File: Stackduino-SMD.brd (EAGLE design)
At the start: 62.5 x 68 mm, 65 parts

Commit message: latest progress on brd v2.1
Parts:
- removed BWD, FWD, MENU_SEL: JST-PH_2-PIN_HEADER, SRG:JST_B2B-PH_HEADER
- removed ENCODER: JST-PH_3-PIN_HEADER, SRG:JST_B3B-PH_HEADER
- removed ICSP: AVR-ISP-6, avr-5:AVR-ISP-6
- added CON1: B4B-ZR, jst-connectors:B4B-ZR
- added U$1: B5B-ZR, jst-connectors:B5B-ZR
- CAM: value JST-PH_3-PIN_HEADER -> B3B-ZR; device SRG:JST_B3B-PH_HEADER -> jst-connectors:B3B-ZR
- U$2: value OLED Display -> B9B-ZR; device Stackduino:DIGOLE_OLED -> jst-connectors:B9B-ZR
- moved H2 78.9 mm to (3.00, 71.0), turned to 180 degrees
- moved H1 78.4 mm to (57.0, 71.0), turned to 180 degrees
- moved 12VDC 76.0 mm to (52.7, 14.9), turned to 180 degrees
- moved USB 74.4 mm to (8.00, 17.0), turned to 90 degrees
- moved H4 70.1 mm to (3.00, 24.2), turned to 180 degrees
- moved H3 63.9 mm to (57.0, 29.0), turned to 180 degrees
- moved L1 62.7 mm to (51.4, 64.3), turned to 180 degrees
- moved R9 61.3 mm to (9.20, 23.6), turned to 0 degrees
- moved D2 58.3 mm to (55.5, 57.8), turned to 90 degrees
- moved CAM 58.0 mm to (11.8, 66.3), turned to 180 degrees
- moved DB15 57.6 mm to (30.0, 17.0), turned to 180 degrees
- moved C8 54.2 mm to (10.1, 39.0), turned to 180 degrees
- moved D1 54.1 mm to (52.6, 29.4), turned to 90 degrees
- moved C10 53.9 mm to (15.3, 29.6)
- moved FT232RL 53.8 mm to (8.45, 32.5), turned to 270 degrees
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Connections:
- removed net N$11: ATMEGA328P.29, C8.1, ICSP.5, R10.1
- new net +5V: U$2.9
- new net RESET: ATMEGA328P.29, C8.1, R10.1, U$2.8
- net BWD: now also CON1.1; no longer BWD.P1
- net CAM_GND: now also CAM.2; no longer CAM.P3
- net ENCSWITCH: now also U$1.5; no longer MENU_SEL.P1
- net ENC_A: now also U$1.1; no longer ENCODER.P1
- net ENC_B: now also U$1.3; no longer ENCODER.P3
- net FWD: now also CON1.3; no longer FWD.P1
- net GND: now also CON1.2, CON1.4, U$1.2, U$1.4, U$2.1; no longer BWD.P2, ENCODER.P2, FWD.P2, ICSP.6, MENU_SEL.P2, U$2.GND@1, U$2.GND@2
- net MISO: now also U$2.6; no longer ICSP.1
- net MOSI: now also U$2.5; no longer ICSP.4
- net N$22: now also U$2.4; no longer U$2.SS
- net N$23: now also U$2.2; no longer U$2.DATA
- net N$24: now also U$2.3; no longer U$2.CLK
- net OPT1: now also CAM.3; no longer CAM.P2
- net OPT2: now also CAM.1; no longer CAM.P1
- net OUT1A: now also A4988_CARRIER.1B; no longer A4988_CARRIER.1A
- net OUT1B: now also A4988_CARRIER.1A; no longer A4988_CARRIER.1B
- net SCK: now also U$2.7; no longer ICSP.3
- net VCC: no longer ICSP.2, U$2.VCC
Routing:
- net VCC: track 457.0 -> 26.8 mm, vias 10 -> 0
- net DIG2: track 146.4 -> 0.00 mm, vias 2 -> 0
- net PBUTTON: track 87.4 -> 0.00 mm, vias 1 -> 0
- net DIG1: track 72.9 -> 0.00 mm, vias 2 -> 0
- net V+: track 86.9 -> 14.4 mm, vias 6 -> 0
- net KILL: track 70.4 -> 0.00 mm, vias 2 -> 0
- net LIM2: track 65.1 -> 0.00 mm, vias 1 -> 0
- net N$11: track 64.8 -> 0.00 mm, vias 2 -> 0
- net STAT: track 57.8 -> 0.00 mm, vias 2 -> 0
- net LIM1: track 56.4 -> 0.00 mm, vias 1 -> 0
- net OPT1: track 68.5 -> 13.8 mm
- net OPT2: track 72.0 -> 21.1 mm
- net N$19: track 49.4 -> 0.00 mm, vias 2 -> 0
- net STEP: track 49.1 -> 0.00 mm
- net CAM_GND: track 67.0 -> 18.1 mm, vias 1 -> 0
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- removed copper zone on layer 1, net VIN
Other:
- board size 62.5 x 68 mm -> 60 x 62 mm

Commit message: latest progress
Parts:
- removed DIG_IO: JST-PH_2-PIN_HEADER, SRG:JST_B2B-PH_HEADER
- added BLUETOOTH: B4B-ZR, jst-connectors:B4B-ZR
- added MP4: NTR4501N, sym:SOT23
- added R18: 2K, eagle-ltspice:R0805
- added R19: 150 Ohm, eagle-ltspice:R0805
- added R22: 10K, eagle-ltspice:R0805
- ON/OFF, START/STOP: value JST-PH_2-PIN_HEADER -> B2B-ZR; device SRG:JST_B2B-PH_HEADER -> jst-connectors:B2B-ZR
- R11: value 10K -> 1K
- moved START/STOP 24.6 mm to (42.0, 72.0)
- moved R5 22.2 mm to (45.0, 51.0)
- moved R3 21.9 mm to (8.45, 55.6)
- moved R11 21.2 mm to (34.0, 52.0), turned to 0 degrees
- moved R4 15.7 mm to (10.4, 55.6)
- moved R12 13.3 mm to (6.50, 41.3), turned to 270 degrees
- moved ON/OFF 12.8 mm to (41.8, 27.9), turned to 180 degrees
- moved R7 12.5 mm to (10.2, 69.8)
- moved OPT1 12.0 mm to (10.2, 66.0), turned to 90 degrees
- moved C13 11.8 mm to (22.4, 66.0)
- moved R6 11.7 mm to (16.5, 63.5), turned to 90 degrees
- moved C1 11.2 mm to (44.5, 28.9), turned to 180 degrees
- moved R14 10.5 mm to (24.4, 53.2)
- moved C5 10.5 mm to (6.50, 50.4), turned to 270 degrees
- moved CAM 10.2 mm to (2.54, 62.2), turned to 90 degrees
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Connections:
- removed net EXTRA_INPUT: DIG_IO.P1, MCP23017.28
- new net BLUETOOTH_ENABLE: MCP23017.28, R19.1
- new net MCU_RX: ATMEGA328P.30, BLUETOOTH.1, FT232RL.1
- new net MCU_TX: ATMEGA328P.31, BLUETOOTH.2, R11.2, R18.1
- new net N$11: FT232RL.5, R11.1
- net GND: now also BLUETOOTH.3, ON/OFF.2, R18.2, R22.1, START/STOP.2; no longer DIG_IO.P2, ON/OFF.P2, START/STOP.P2
- net N$13: now also MP4.1, R19.2, R22.2; no longer ATMEGA328P.31, FT232RL.5
- net N$14: now also BLUETOOTH.4, MP4.2; no longer ATMEGA328P.30, FT232RL.1
- net OPT1: now also CAM.1; no longer CAM.3
- net OPT2: now also CAM.3; no longer CAM.1
- net PBUTTON: now also ON/OFF.1; no longer ON/OFF.P1, R11.1
- net START_STOP: now also START/STOP.1; no longer START/STOP.P1
- net V+: no longer R11.2
- net VCC: now also MP4.3
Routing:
- net VCC: track 26.8 -> 121.5 mm
- net LIM1: track 0.00 -> 46.3 mm
- net CAM_GND: track 18.1 -> 61.2 mm
- net LIM2: track 0.00 -> 42.2 mm
- net STEP: track 0.00 -> 41.6 mm, vias 0 -> 1
- net MCU_RX: track 0.00 -> 41.3 mm, vias 0 -> 1
- net OPT1: track 13.8 -> 52.4 mm, vias 1 -> 0
- net DIR: track 0.00 -> 37.8 mm, vias 0 -> 1
- net DIG1: track 0.00 -> 35.6 mm, vias 0 -> 1
- net DIG2: track 0.00 -> 35.0 mm, vias 0 -> 1
- net ENCSWITCH: track 0.00 -> 34.0 mm, vias 0 -> 1
- net N$11: track 0.00 -> 32.7 mm, vias 0 -> 1
- net OPT2: track 21.1 -> 53.6 mm, vias 1 -> 0
- net N$19: track 0.00 -> 31.8 mm, vias 0 -> 2
- net N$18: track 0.00 -> 30.0 mm, vias 0 -> 2
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
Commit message: topside board nearly complete
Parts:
- removed LTC2950: LTC2950CTS8-1TRPBF, LTC_By_element14_Batch_1:SOT65P280X100-8N
- removed LTC4412: LTC4412ES6PBF, LTC_By_element14_Batch_1:SOT95P280X100-6N
- removed R0: 470K, eagle-ltspice:R0805
- removed R22: 10K, eagle-ltspice:R0805
- added LTC1: LTC2950CTS8-1TRPBF, LTC_By_element14_Batch_1:SOT65P280X100-8N
- added LTC2: LTC4412ES6PBF, LTC_By_element14_Batch_1:SOT95P280X100-6N
- added R20: 4.7K, eagle-ltspice:R0805
- added R21: 100K, eagle-ltspice:R0805
- C1: value 22uF -> 0.1uF
- C10: value 100nF -> 0.1uF
- C11: value 22pF -> 100uF; device eagle-ltspice:C0805 -> SparkFun-Passives:PANASONIC_D
- C12: value 22pF -> 100nF
- C13: value 0.1uF -> 22uF
- C2: value 100uF -> 22pF; device SparkFun-Passives:PANASONIC_D -> eagle-ltspice:C0805
- C3: value 10nF -> 22pF
- C4: value 68uF -> 10nF; device SparkFun-Passives:PANASONIC_D -> eagle-ltspice:C0805
- C6: value 100uF -> 68uF
- C7: value 0.1uF -> 100uF; device eagle-ltspice:C0805 -> SparkFun-Passives:PANASONIC_D
- MP1: value FDN306P -> NTR4501N
- MP4: value NTR4501N -> FDN306P
- R1, R2: value 100K -> 220 Ohm
- R10, R16: value 10K -> 150 Ohm
- R12: value 10K -> 2K
- R13, R19: value 150 Ohm -> 10K
- R14: value 10K -> 470K
- R15, R3, R9: value 4.7K -> 10K
- R17: value 150 Ohm -> 100K
- R18: value 2K -> 100K
- R4: value 4.7K -> 150 Ohm
- R5: value 100K -> 4.7K
- R6: value 220 Ohm -> 4.7K
- R7: value 220 Ohm -> 10K
- R8: value 10K -> 4.7K
- moved H3 54.2 mm to (3.00, 24.2)
- moved H4 54.2 mm to (57.0, 29.0)
- moved H1 54.0 mm to (3.00, 71.0)
- moved H2 54.0 mm to (57.0, 71.0)
- moved R1 51.7 mm to (10.2, 70.5), turned to 180 degrees
- moved MP4 50.2 mm to (52.0, 38.4), turned to 270 degrees
- moved C13 46.9 mm to (46.9, 26.0), turned to 270 degrees
- moved C12 46.5 mm to (18.5, 28.9), turned to 0 degrees
- moved R2 45.0 mm to (16.5, 63.5), turned to 90 degrees
- moved MP1 44.8 mm to (5.20, 56.4), turned to 0 degrees
- moved C1 43.2 mm to (22.4, 66.0), turned to 90 degrees
- moved R5 36.8 mm to (8.45, 55.6)
- moved R8 33.3 mm to (24.4, 55.6), turned to 0 degrees
- moved R9 33.3 mm to (24.4, 53.2), turned to 180 degrees
- moved R12 32.4 mm to (36.8, 52.8), turned to 90 degrees
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- renumbered CON1 to FWD/BWD, DB15 to DB1, LM2675 to LM1, MCP23017 to MCP1, U$1 to ENCODER, U$2 to ICSP/SPI/OLED
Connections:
- net BATTVIN: now also LTC2.1, MP4.3; no longer LTC4412.1, MP1.3
- net BATT_FET: now also R10.1; no longer R13.1
- net BATT_SENSE: now also R8.2, R9.1; no longer R14.1, R15.2
- net BATT_VOLT: now also MP2.3; no longer MP3.3
- net BLUETOOTH_ENABLE: now also R4.1; no longer R19.1
- net GATE: now also LTC2.5, MP4.1; no longer LTC4412.5, MP1.1
- net GND: now also C11.-, C2.2, C3.2, C7.-, D1.A, LTC1.4, LTC2.2, LTC2.3, R12.2, R19.2, R3.1, R7.1, R8.1; no longer C11.2, C2.-, C4.-, C7.2, D2.A, LTC2950.4, LTC4412.2, LTC4412.3, R15.1, R16.1, R18.2, R22.1, R8.2
- net INT: now also LTC1.5, R18.2; no longer LTC2950.5, R2.2
- net KILL: now also LTC1.8, R21.1; no longer LTC2950.8, R1.1
- net MCU_TX: now also R12.1; no longer R18.1
- net N$1: now also LTC1.6; no longer LTC2950.6
- net N$10: now also MP3.1, R16.1; no longer MP2.1, R17.1
- net N$12: now also MP2.1, R10.2, R7.2; no longer MP3.1, R13.2, R16.2
- net N$13: now also MP1.1, R3.2, R4.2; no longer MP4.1, R19.2, R22.2
- net N$14: now also MP1.2; no longer MP4.2
- net N$16: now also MP2.2, R9.2; no longer MP3.2, R14.2
- net N$18: now also R6.1; no longer R4.1
- net N$19: now also R5.2; no longer R3.2
- net N$2: now also R17.1; no longer R5.1
- net N$30: now also R20.1; no longer R9.1
- net N$34: now also R2.1; no longer R6.1
- net N$36: now also R1.1; no longer R7.1
- net N$4: now also C4.1; no longer C3.1
- net N$43: now also C12.1; no longer C10.1
- net N$44: now also R19.1, R20.2; no longer R8.1, R9.2
- net N$7: now also C4.2, D1.C; no longer C3.2, D2.C
- net N$8: now also R13.1; no longer R12.1
- net N$9: now also C11.+, MP3.2; no longer MP2.2
- net PBUTTON: now also LTC1.2; no longer LTC2950.2
- net PD6: now also R2.2; no longer R6.2
- net PD7: now also R1.2; no longer R7.2
- net RESET: now also R15.1; no longer R10.1
- net STAT: now also LTC2.4, R14.1; no longer LTC4412.4, R0.1
- net V+: now also C13.1, C7.+, D2.C, LTC1.1, LTC2.6, MP3.3, MP4.2; no longer C1.1, C2.+, C6.+, D1.C, LTC2950.1, LTC4412.6, MP1.2, MP2.3
- net VCC: now also C1.1, C10.1, C6.+, MP1.3, R13.2, R14.2, R15.2, R16.2, R18.1, R21.2, R5.1, R6.2; no longer C13.1, C4.+, C7.1, MP4.3, R0.2, R1.2, R10.2, R12.2, R2.1, R3.1, R4.2, R5.2
- net VIN: now also D2.A; no longer D1.A
- net XTAL1: now also C3.1; no longer C11.1
- net XTAL2: now also C2.1; no longer C12.1
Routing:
- net MCU_TX: track 7.92 -> 73.0 mm, vias 0 -> 2
- net RESET: track 7.72 -> 69.4 mm, vias 0 -> 3
- net VCC: track 121.5 -> 180.3 mm, vias 0 -> 4
- net DIG1: track 35.6 -> 1.84 mm, vias 1 -> 0
- net DIG2: track 35.0 -> 1.57 mm, vias 1 -> 0
- net MCU_RX: track 41.3 -> 7.91 mm, vias 1 -> 0
- net ENCSWITCH: track 34.0 -> 2.63 mm, vias 1 -> 0
- net N$11: track 32.7 -> 1.45 mm, vias 1 -> 0
- net N$17: track 27.2 -> 1.47 mm, vias 1 -> 0
- net N$1: track 0.00 -> 24.6 mm, vias 0 -> 2
- net N$14: track 24.0 -> 1.68 mm, vias 1 -> 0
- net PD6: track 32.6 -> 45.6 mm, vias 2 -> 0
- net V+: track 20.9 -> 33.0 mm
- net BATTVIN: track 0.00 -> 11.9 mm
- net GATE: track 0.00 -> 11.1 mm, vias 0 -> 2
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- added copper zone on layer 1, net BATTVIN
- added copper zone on layer 1, net N$9
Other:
- board text removed: "MISO"
- board text removed: "MOSI"
- board text removed: "RST"
- board text removed: "SCK"
- board text removed: "VDD"

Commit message: latest progress
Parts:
- moved R14 7.13 mm to (11.9, 39.6)
- moved C10 3.42 mm to (33.0, 29.8), turned to 270 degrees
- moved CAM 0.46 mm to (3.00, 62.2)
- moved FWD/BWD 0.10 mm to (1.50, 41.2)
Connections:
- net DIG1: now also DB1.14; no longer DB1.13
- net DIG2: now also DB1.13; no longer DB1.14
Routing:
- net DIG2: track 1.57 -> 50.8 mm
- net DIG1: track 1.84 -> 46.6 mm
- net OPT2: track 59.4 -> 68.8 mm
- net OPT1: track 59.6 -> 68.0 mm
- net CAM_GND: track 67.0 -> 73.3 mm
- net N$2: track 5.26 -> 0.00 mm
- net DIR: track 34.6 -> 39.4 mm
- net STEP: track 38.4 -> 42.5 mm
- net LIM1: track 46.3 -> 49.8 mm
- net LIM2: track 42.2 -> 45.6 mm
- net VCC: track 180.3 -> 177.1 mm
- net SLEEP: track 23.9 -> 22.6 mm, vias 0 -> 1
- net MS3: track 18.9 -> 17.8 mm
- net RESET: track 69.4 -> 68.2 mm
- net ENABLE: track 16.6 -> 15.6 mm
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
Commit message: nearly there,,,
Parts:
- moved R14 41.9 mm to (47.0, 16.6), turned to 270 degrees
- moved C8 7.18 mm to (11.1, 39.3), turned to 180 degrees
- moved C9 2.34 mm to (16.6, 32.8), turned to 270 degrees
- moved R17 2.05 mm to (31.8, 36.2)
- moved C12 1.95 mm to (16.6, 28.9), turned to 270 degrees
- moved C10 1.80 mm to (31.8, 31.1), turned to 180 degrees
- moved R4 1.62 mm to (2.27, 51.4)
- moved R7 1.56 mm to (15.2, 55.5), turned to 0 degrees
- moved MP2 1.45 mm to (19.3, 56.6)
- moved FT232RL 1.34 mm to (10.1, 32.8)
- moved C2 0.80 mm to (41.2, 70.3)
- moved C3 0.80 mm to (41.2, 55.2)
- moved H1 0.80 mm to (3.00, 71.8)
- moved H2 0.80 mm to (57.0, 71.8)
- moved START/STOP 0.75 mm to (43.5, 72.2)
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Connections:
- net N$14 renamed BLUETOOTH_VCC
- removed net N$11: FT232RL.5, R11.1
- new net MCU_TX_3_3V: BLUETOOTH.2, FT232RL.5, R11.1
- net DIG1: now also DB1.12; no longer DB1.14
- net DIG2: now also DB1.11; no longer DB1.13
- net ENCSWITCH: now also MCP1.3; no longer MCP1.26
- net INT: now also MCP1.24; no longer MCP1.27
- net KILL: now also MCP1.25; no longer MCP1.3
- net LIM1: now also DB1.13, MCP1.26; no longer DB1.11, MCP1.23
- net LIM2: now also DB1.14, MCP1.27; no longer DB1.12, MCP1.24
- net MCU_TX: no longer BLUETOOTH.2
- net PD6: now also ATMEGA328P.11; no longer ATMEGA328P.10
- net PD7: now also ATMEGA328P.10; no longer ATMEGA328P.11
- net STAT: now also MCP1.23; no longer MCP1.25
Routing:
- net STAT: track 3.96 -> 74.8 mm, vias 0 -> 2
- net BATT_VOLT: track 9.26 -> 76.4 mm
- net ALOG2: track 2.27 -> 67.5 mm, vias 0 -> 1
- net ALOG1: track 2.27 -> 67.1 mm, vias 0 -> 1
- net MCU_TX: track 73.0 -> 8.62 mm, vias 2 -> 0
- net INT: track 6.35 -> 68.1 mm, vias 0 -> 2
- net KILL: track 8.89 -> 62.7 mm
- net MCU_TX_3_3V: track 0.00 -> 37.8 mm, vias 0 -> 2
- net MCU_RX: track 7.91 -> 38.1 mm, vias 0 -> 2
- net BLUETOOTH_VCC: track 1.68 -> 28.8 mm, vias 0 -> 1
- net N$17: track 1.47 -> 27.1 mm, vias 0 -> 2
- net ENCSWITCH: track 2.63 -> 22.4 mm, vias 0 -> 1
- net VCC: track 177.1 -> 162.1 mm, vias 4 -> 3
- net PD7: track 29.5 -> 44.4 mm, vias 2 -> 0
- net N$2: track 0.00 -> 14.9 mm, vias 0 -> 1
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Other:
- board size 60 x 62 mm -> 60 x 62.8 mm

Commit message: latest progress
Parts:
- moved R14 33.5 mm to (77.4, 30.7), turned to 180 degrees
- moved MP1 2.88 mm to (3.25, 54.3)
- moved R3 2.34 mm to (4.00, 57.8), turned to 180 degrees
- moved FWD/BWD 1.50 mm to (1.50, 39.8)
- moved OPT1 1.27 mm to (11.4, 66.0)
- moved OPT2 1.27 mm to (11.4, 61.0)
- moved R2 1.27 mm to (17.8, 63.5)
- moved R4 0.98 mm to (2.27, 50.4)
- moved R16 0.65 mm to (40.8, 46.1)
- moved R12 0.45 mm to (37.2, 53.0)
- moved R15 0.28 mm to (33.8, 49.8)
- moved R11 0.20 mm to (33.8, 52.0)
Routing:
- net VCC: track 162.1 -> 176.6 mm, vias 3 -> 5
- net MCU_TX_3_3V: track 37.8 -> 48.5 mm
- net ALOG2: track 67.5 -> 72.2 mm
- net ALOG1: track 67.1 -> 71.5 mm
- net STEP: track 44.5 -> 48.3 mm
- net N$13: track 6.36 -> 9.12 mm
- net BLUETOOTH_VCC: track 28.8 -> 26.8 mm
- net N$2: track 14.9 -> 16.6 mm
- net PD6: track 47.8 -> 49.3 mm
- net N$36: track 7.66 -> 9.10 mm
- net N$17: track 27.1 -> 28.5 mm
- net RESET: track 60.2 -> 58.8 mm
- net OPT2: track 68.9 -> 70.2 mm
- net OPT1: track 69.7 -> 71.0 mm
- net FWD: track 12.3 -> 13.5 mm
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
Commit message: latest progress
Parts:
- moved R14 38.3 mm to (39.2, 28.0)
- moved ON/OFF 3.32 mm to (42.3, 27.9), turned to 90 degrees
- moved C7 1.62 mm to (55.7, 45.4)
- moved C6 1.31 mm to (47.8, 48.4)
- moved R21 1.08 mm to (39.2, 30.0), turned to 180 degrees
- moved R18 0.79 mm to (38.4, 33.8)
- moved D1 0.69 mm to (55.9, 55.6)
- moved C13 0.67 mm to (46.8, 26.6)
- moved C2 0.60 mm to (41.2, 69.7)
- moved C3 0.60 mm to (41.2, 55.8)
- moved D2 0.40 mm to (50.5, 30.0)
- moved LTC1 0.32 mm to (43.5, 33.8)
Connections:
- net GND: now also ON/OFF.1; no longer ON/OFF.2
- net PBUTTON: now also ON/OFF.2; no longer ON/OFF.1
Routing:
- net V+: track 25.0 -> 13.4 mm
- net STAT: track 74.8 -> 83.4 mm
- net KILL: track 62.7 -> 64.9 mm, vias 0 -> 2
- net INT: track 68.1 -> 70.2 mm
- net VCC: track 176.6 -> 178.3 mm
- net XTAL1: track 10.6 -> 9.98 mm
- net XTAL2: track 10.5 -> 9.91 mm
- net GND: vias 3 -> 4

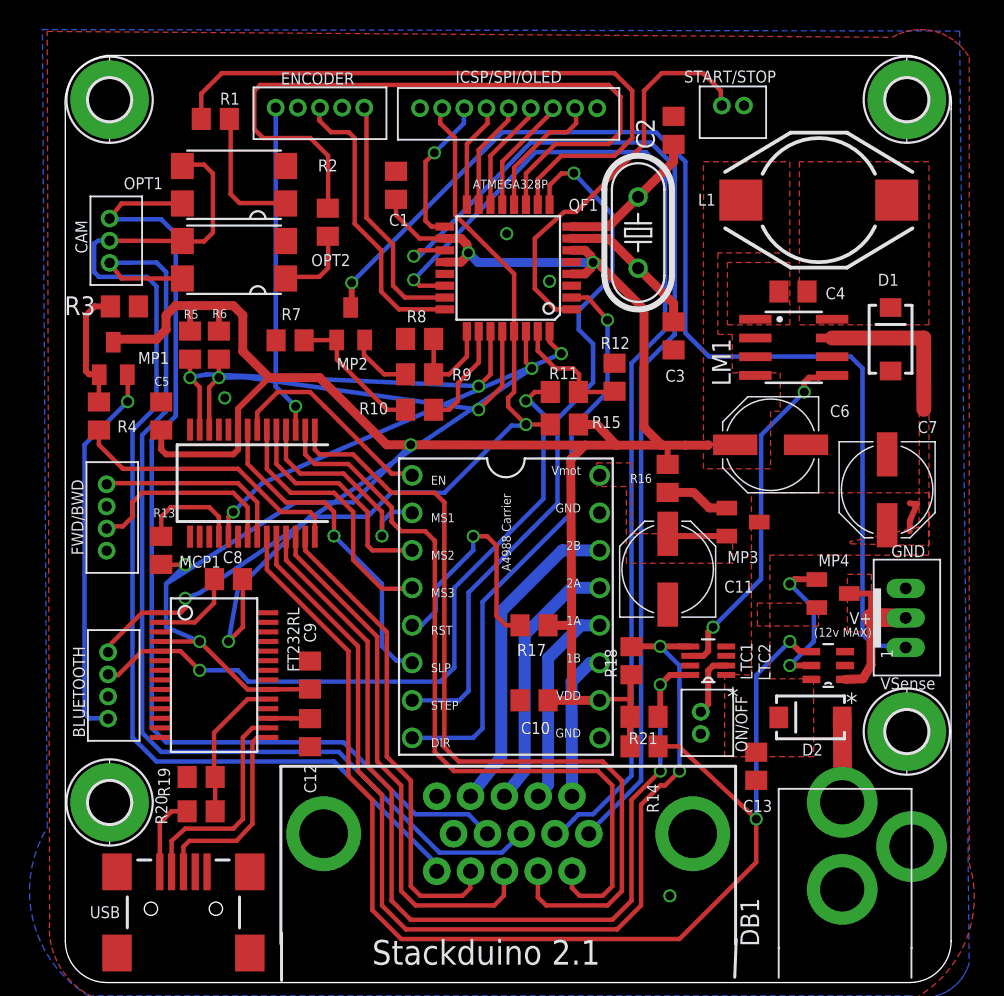
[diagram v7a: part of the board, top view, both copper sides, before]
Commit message: no errors in DRC!
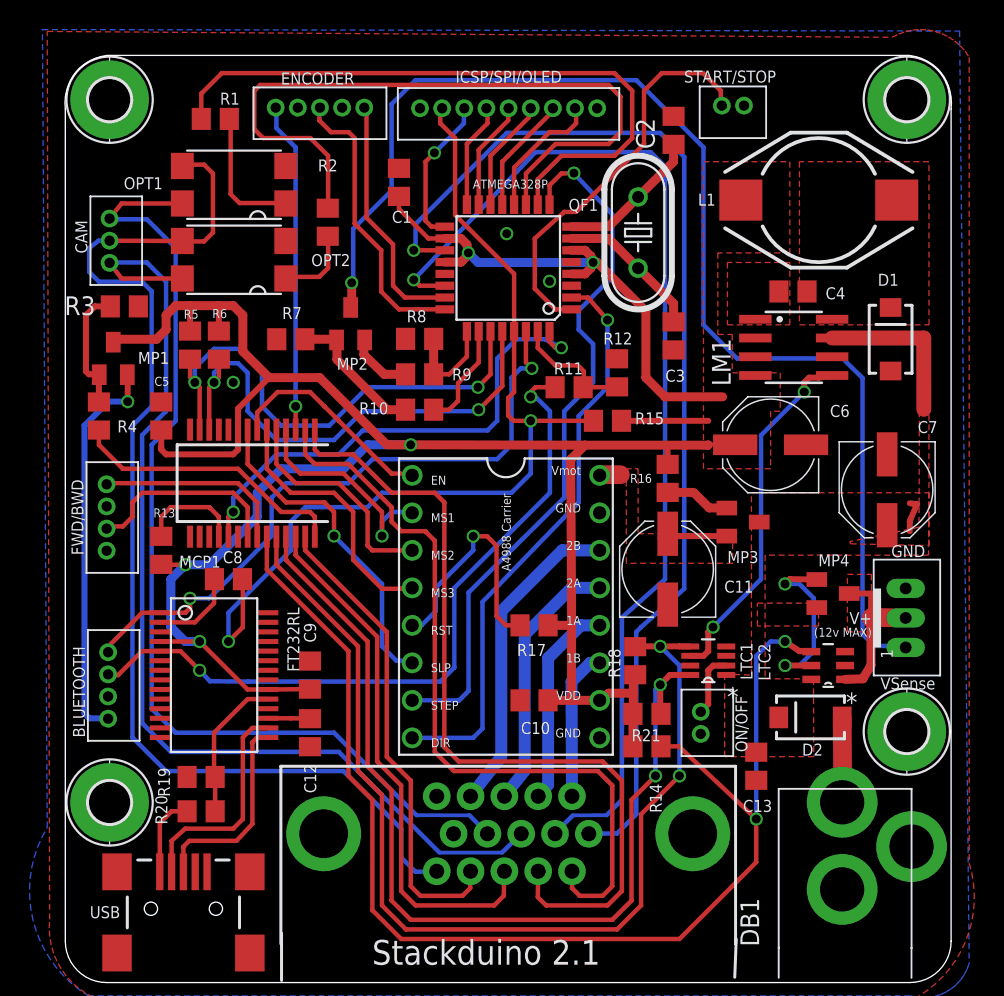
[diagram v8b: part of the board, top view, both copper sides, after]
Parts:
- moved R15 2.94 mm to (36.7, 50.0)
- moved R11 0.46 mm to (34.1, 52.3)
- moved R12 0.35 mm to (37.4, 53.3)
- moved C1 0.28 mm to (22.6, 66.2)
- moved R21 0.28 mm to (39.4, 30.2)
- moved R18 0.25 mm to (38.6, 33.8)
- moved R14 0.20 mm to (39.4, 28.0)
- moved R7 0.09 mm to (15.3, 55.6)
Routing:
- net BATT_VOLT: track 76.3 -> 84.6 mm
- net RESET: track 58.8 -> 65.0 mm
- net N$19: track 29.3 -> 35.2 mm
- net MCU_RX: track 38.2 -> 44.1 mm
- net N$18: track 29.3 -> 35.0 mm
- net N$17: track 28.5 -> 33.7 mm
- net ALOG1: track 71.5 -> 75.1 mm
- net VCC: track 178.3 -> 181.5 mm
- net GATE: track 10.8 -> 12.3 mm
- net N$9: track 7.79 -> 9.19 mm
- net OPT2: track 70.2 -> 68.8 mm
- net ALOG2: track 72.2 -> 73.1 mm
- net MCU_TX_3_3V: track 48.5 -> 49.3 mm
- net BLUETOOTH_VCC: track 26.8 -> 27.6 mm
- net OPT1: track 71.0 -> 70.2 mm
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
